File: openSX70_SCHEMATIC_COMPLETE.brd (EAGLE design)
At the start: 95.9 x 27.9 mm, 41 parts, among them Q1 5.8A/30V/35mΩ, Q2 5.8A/30V/35mΩ, U1 ATMEGA328P_TQFP, U3 BH1750FVI-TR, Y1 16MHz

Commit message: Eagle openSX70 pcb layout 2.0
Layout 2.0
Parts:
- removed BUZZ1: CSET8-5G, CSET8-5G_B:CSET8-5G_PACKAGE
- removed J1: (no value), SparkFun-Connectors:1X06
- removed U3: BH1750FVI-TR, openSX70:SOTFL50P300X75-6N
- added BH1750: BH1750FVI-TR, openSX70:SOTFL50P300X75-6N
- added BUZZER: CSET8-5G, CSET8-5G_B:CSET8-5G_PACKAGE
- added FTDI: FTDI HEADER, SparkFun-Connectors:1X06
- S1+, S1-, S2+, S2-, SOL2+, SOL2-: value SX70_S-PAD -> SX70-S-PAD-NEW; device openSX70:SX70-S-PAD -> openSX70:SX70-S-PAD2
- moved C4 51.6 mm to (15.1, 22.4), flipped to the bottom
- moved C3 42.6 mm to (19.3, 18.3), flipped to the bottom, turned to 180 degrees
- moved R6 31.0 mm to (96.6, 14.9), turned to 90 degrees
- moved R5 28.4 mm to (96.6, 11.7), turned to 90 degrees
- moved R10 21.8 mm to (95.6, 18.7)
- moved R3 19.7 mm to (76.1, 26.0), turned to 0 degrees
- moved Q2 18.6 mm to (76.2, 22.9), turned to 270 degrees
- moved R1 17.9 mm to (67.8, 21.7), turned to 180 degrees
- moved C7 17.8 mm to (27.9, 3.81), turned to 180 degrees
- moved R12 17.5 mm to (24.1, 3.81)
- moved R2 15.6 mm to (67.8, 23.7), turned to 180 degrees
- moved R4 15.2 mm to (71.4, 23.7)
- moved C1 14.9 mm to (15.5, 19.1)
- moved R9 14.4 mm to (95.6, 17.1), turned to 180 degrees
- moved C2 13.9 mm to (16.5, 12.7), turned to 180 degrees
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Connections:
- removed net N$9 (its old number): C5.1, R13.1, U3.5
- new net N$2: BH1750.5, C5.1, R13.1
- net 3.3V: now also BH1750.1, FTDI.4; no longer J1.4, U3.1
- net BUZZER: now also BUZZER.+
- net DTR: now also FTDI.1; no longer J1.1
- net GND: now also BH1750.3, BUZZER.GND-, FTDI.6; no longer J1.6, U3.3
- net N$10: now also BH1750.2; no longer U3.2
- net RXD: now also FTDI.3; no longer J1.3
- net SCL: now also BH1750.6; no longer U3.6
- net SDA: now also BH1750.4; no longer U3.4
- net TXD: now also FTDI.2; no longer J1.2
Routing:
- net 3.3V: track 0.00 -> 123.8 mm, vias 0 -> 4
- net LED: track 0.00 -> 105.1 mm, vias 0 -> 1
- net BUZZER: track 0.00 -> 89.1 mm, vias 0 -> 5
- net SCL: track 0.00 -> 83.0 mm, vias 0 -> 2
- net N$4: track 0.00 -> 80.9 mm, vias 0 -> 2
- net SDA: track 0.00 -> 74.3 mm, vias 0 -> 3
- net N$6: track 0.00 -> 67.4 mm, vias 0 -> 3
- net N$9: track 0.00 -> 66.1 mm, vias 0 -> 2
- net FF: track 0.00 -> 60.5 mm, vias 0 -> 2
- net TXD: track 0.00 -> 44.4 mm, vias 0 -> 1
- net RXD: track 0.00 -> 42.5 mm, vias 0 -> 1
- net N$11: track 24.5 -> 0.00 mm, vias 2 -> 0
- net 6V: track 119.4 -> 142.3 mm
- net S5: track 0.00 -> 22.1 mm, vias 0 -> 2
- net N$1: track 0.00 -> 21.9 mm
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- added copper zone on layer 1, net N$11
- added copper zone on layer 1, net N$12
- added copper zone on layer 1, net N$13
- added copper zone on layer 1, net N$14
- added copper zone on layer 1, net N$16
- added copper zone on layer 1, net N$17
- added copper zone on layer 16, net N$18
- added copper zone on layer 16, net N$19
- added copper zone on layer 16, net N$20
- added copper zone on layer 16, net N$21
- added copper zone on layer 16, net N$22
- added copper zone on layer 16, net N$23
- added copper zone on layer 16, net N$24
- added copper zone on layer 16, net N$25
- added copper zone on layer 1, net N$7
- added copper zone on layer 1, net N$8
- removed copper zone on layer 16, net S$11
- removed copper zone on layer 16, net S$12
- removed copper zone on layer 16, net S$13
- removed copper zone on layer 16, net S$14
- removed copper zone on layer 16, net S$15
- removed copper zone on layer 16, net S$16
- removed copper zone on layer 16, net S$17
- removed copper zone on layer 16, net S$18
- removed copper zone on layer 1, net S$2
- removed copper zone on layer 1, net S$3
- removed copper zone on layer 1, net S$4
- removed copper zone on layer 1, net S$5
- removed copper zone on layer 1, net S$6
- removed copper zone on layer 1, net S$7
- removed copper zone on layer 1, net S$8
- removed copper zone on layer 1, net S$9
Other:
- outline, holes or cut-outs redrawn
- board text added: "+"
- board text added: "-"
- board text added: "CUT OUT"
- board text added: "F+"
- board text added: "F-"
- board text added: "FF"
- board text added: "GND"
- board text added: "LD1117@3.3V"
- board text added: "MOTOR"
- board text added: "S1+"
- board text added: "S1-"
- board text added: "S2+"
- board text added: "S2-"
- board text added: "S3"
- board text added: "S5"
- board text added: "S8"
- board text added: "S9"
- board text added: "SOL#2+"
- board text added: "SOL#2-"
- board text added: "VCC-6V"
- board text added: "bottom"
- board text added: "layout 2.0"
- board text added: "openSX70.com"
- board text added: "top"

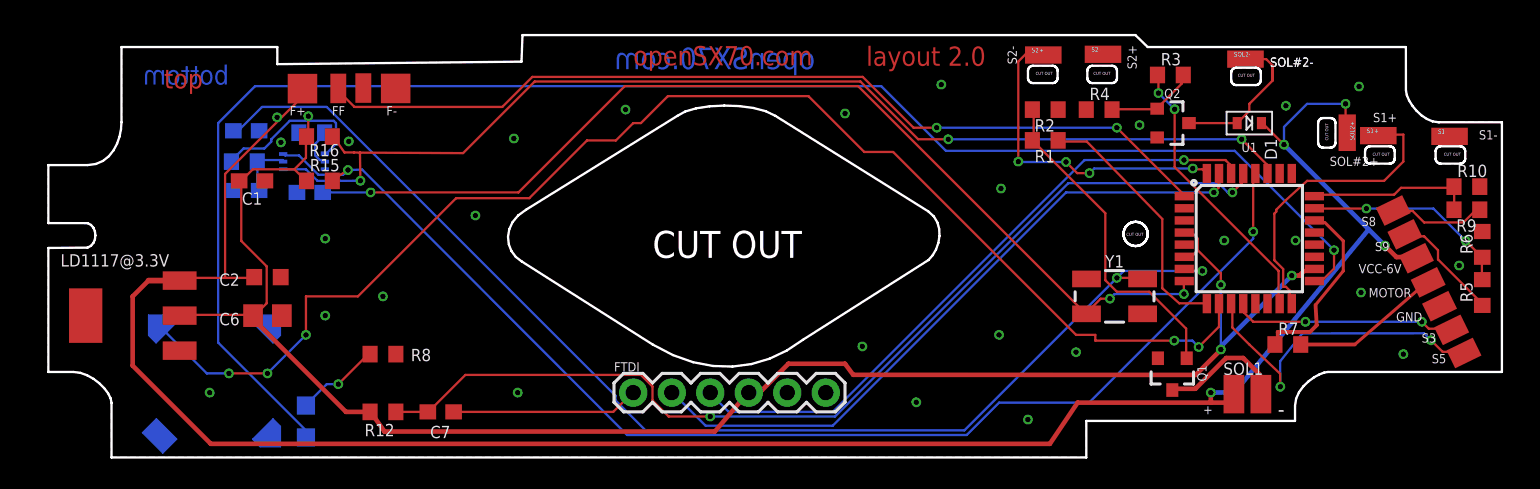
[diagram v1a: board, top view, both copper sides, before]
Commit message: Eagle main PCB 2.1
Eagle main PCB 2.1, manufactured by EasyEDA as a test 26/11/2017
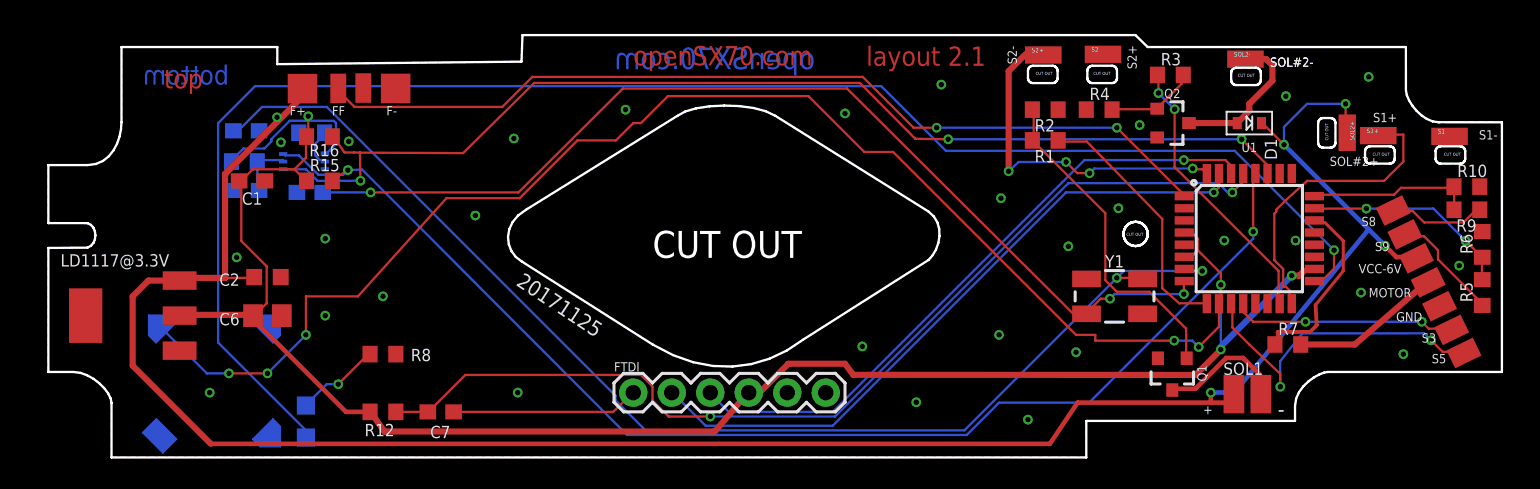
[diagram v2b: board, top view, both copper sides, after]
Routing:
- net S2: track 21.5 -> 23.3 mm
- net GND: vias 27 -> 30
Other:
- board text added: "20171125"
- board text added: "layout 2.1"
- board text removed: "layout 2.0"
